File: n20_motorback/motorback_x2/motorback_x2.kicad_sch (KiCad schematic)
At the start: 13 parts, among them J1 Servo wire input, J2 Conn_01x01_Male, J3 Conn_01x01_Male, J4 prog_pins, U1 DRV8837DSGR, U2 ATtiny4-TS, U3 AIC1734-33GUTR

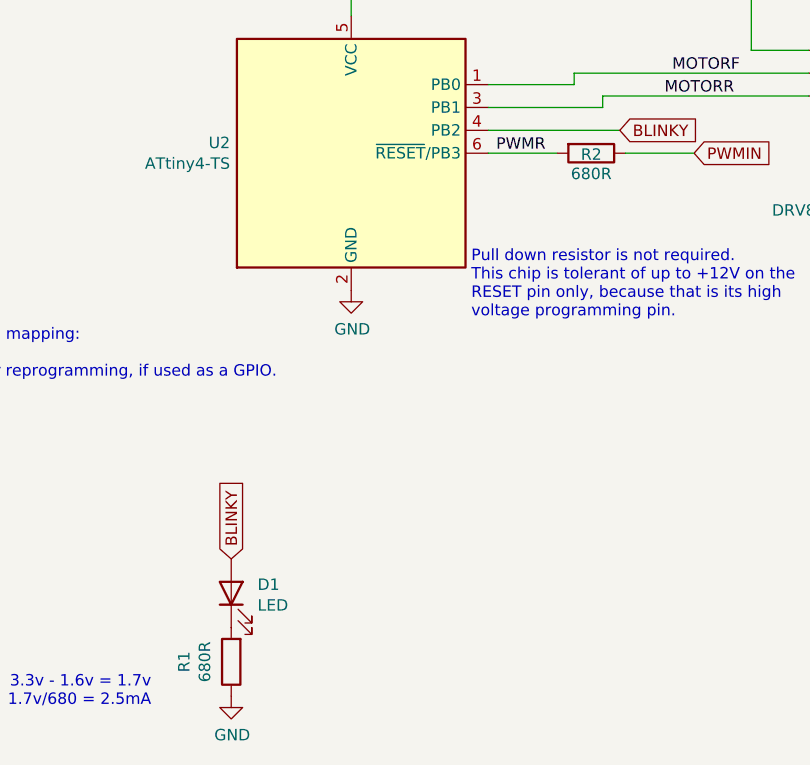
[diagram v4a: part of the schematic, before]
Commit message: Use 1k resistors
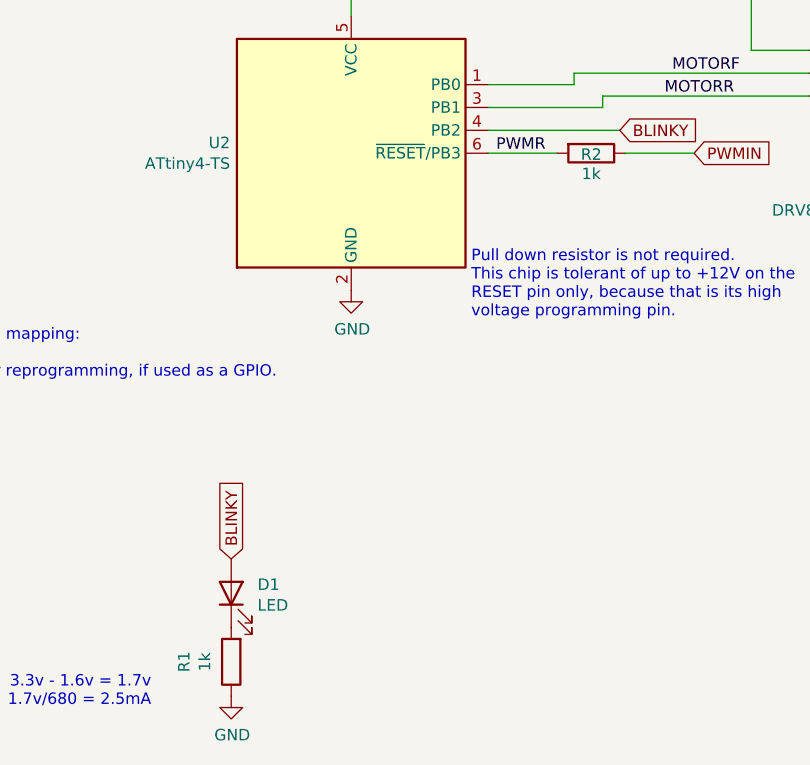
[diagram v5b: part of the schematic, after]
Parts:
- R1, R2: value 680R -> 1k; LCSC C23228 -> C21190
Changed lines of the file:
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@@
-(kicad_sch (version 20201015) (generator eeschema)
+(kicad_sch (version 20210126) (generator eeschema)
   (paper "A4")
   (title_block
@@
     (effects (font (size 1.27 1.27)) (justify left bottom))
   )
-  (global_label "PWMIN" (shape input) (at 40.64 43.18 0)    (property "Intersheet References" "${INTERSHEET_REFS}" (id 0) (at -12.7 -5.08 0)
-      (effects (font (size 1.27 1.27)) hide)
-    )
+  (global_label "PWMIN" (shape input) (at 40.64 43.18 0)
     (effects (font (size 1.27 1.27)) (justify left))
-  )
-  (global_label "PWMIN" (shape input) (at 44.45 86.36 0)    (property "Intersheet References" "${INTERSHEET_REFS}" (id 0) (at -8.89 38.1 0)
-      (effects (font (size 1.27 1.27)) hide)
-    )
+    (property "Intersheet References" "${INTERSHEET_REFS}" (id 0) (at -12.7 -5.08 0)
+      (effects (font (size 1.27 1.27)) hide)
+    )
+  )
+  (global_label "PWMIN" (shape input) (at 44.45 86.36 0)
     (effects (font (size 1.27 1.27)) (justify left))
-  )
-  (global_label "VBAT" (shape input) (at 66.04 38.1 90)    (property "Intersheet References" "${INTERSHEET_REFS}" (id 0) (at 0 0 0)
-      (effects (font (size 1.27 1.27)) hide)
-    )
+    (property "Intersheet References" "${INTERSHEET_REFS}" (id 0) (at -8.89 38.1 0)
+      (effects (font (size 1.27 1.27)) hide)
+    )
+  )
+  (global_label "VBAT" (shape input) (at 66.04 38.1 90)
     (effects (font (size 1.27 1.27)) (justify left))
-  )
-  (global_label "BLINKY" (shape input) (at 142.875 135.255 90)    (property "Intersheet References" "${INTERSHEET_REFS}" (id 0) (at 142.7956 124.726 90)
+    (property "Intersheet References" "${INTERSHEET_REFS}" (id 0) (at 0 0 0)
+      (effects (font (size 1.27 1.27)) hide)
+    )
+  )
+  (global_label "BLINKY" (shape input) (at 142.875 135.255 90)
+    (effects (font (size 1.27 1.27)) (justify left))
+    (property "Intersheet References" "${INTERSHEET_REFS}" (id 0) (at 142.7956 124.726 90)
       (effects (font (size 1.27 1.27)) (justify left) hide)
     )
+  )
+  (global_label "BLINKY" (shape input) (at 186.055 87.63 0)
     (effects (font (size 1.27 1.27)) (justify left))
-  )
-  (global_label "BLINKY" (shape input) (at 186.055 87.63 0)    (property "Intersheet References" "${INTERSHEET_REFS}" (id 0) (at 196.584 87.5506 0)
+    (property "Intersheet References" "${INTERSHEET_REFS}" (id 0) (at 196.584 87.5506 0)
       (effects (font (size 1.27 1.27)) (justify left) hide)
     )
+  )
+  (global_label "PWMIN" (shape input) (at 194.31 90.17 0)
     (effects (font (size 1.27 1.27)) (justify left))
-  )
-  (global_label "PWMIN" (shape input) (at 194.31 90.17 0)    (property "Intersheet References" "${INTERSHEET_REFS}" (id 0) (at 22.86 2.54 0)
-      (effects (font (size 1.27 1.27)) hide)
-    )
+    (property "Intersheet References" "${INTERSHEET_REFS}" (id 0) (at 22.86 2.54 0)
+      (effects (font (size 1.27 1.27)) hide)
+    )
+  )
+  (global_label "VBAT" (shape input) (at 233.045 58.42 0)
     (effects (font (size 1.27 1.27)) (justify left))
-  )
-  (global_label "VBAT" (shape input) (at 233.045 58.42 0)    (property "Intersheet References" "${INTERSHEET_REFS}" (id 0) (at 301.625 -158.75 0)
-      (effects (font (size 1.27 1.27)) hide)
-    )
-    (effects (font (size 1.27 1.27)) (justify left))
+    (property "Intersheet References" "${INTERSHEET_REFS}" (id 0) (at 301.625 -158.75 0)
+      (effects (font (size 1.27 1.27)) hide)
+    )
   )
   (symbol (lib_id "power:PWR_FLAG") (at 55.88 48.26 180) (unit 1)
@@
       (effects (font (size 1.27 1.27)) hide)
     )
+    (pin "1")
   )
   (symbol (lib_id "power:PWR_FLAG") (at 74.93 43.18 0) (unit 1)
@@
       (effects (font (size 1.27 1.27)) hide)
     )
+    (pin "1")
   )
   (symbol (lib_id "power:GND") (at 41.275 95.25 0) (unit 1)
@@
       (effects (font (size 1.27 1.27)) hide)
     )
+    (pin "1")
   )
   (symbol (lib_id "power:GND") (at 43.18 37.465 0) (unit 1)
@@
       (effects (font (size 1.27 1.27)) hide)
     )
+    (pin "1")
   )
   (symbol (lib_id "power:GND") (at 64.135 48.26 0) (unit 1)
@@
       (effects (font (size 1.27 1.27)) hide)
     )
+    (pin "1")
   )
   (symbol (lib_id "power:GND") (at 142.875 150.495 0) (unit 1)
@@
       (effects (font (size 1.27 1.27)) hide)
     )
+    (pin "1")
   )
   (symbol (lib_id "power:GND") (at 156.21 105.41 0) (unit 1)
@@
       (effects (font (size 1.27 1.27)) hide)
     )
+    (pin "1")
   )
   (symbol (lib_id "power:GND") (at 217.17 93.98 0) (unit 1)
@@
       (effects (font (size 1.27 1.27)) hide)
     )
+    (pin "1")
   )
   (symbol (lib_id "power:GND") (at 224.155 66.04 0) (unit 1)
@@
       (effects (font (size 1.27 1.27)) hide)
     )
+    (pin "1")
   )
   (symbol (lib_id "Connector:Conn_01x01_Male") (at 252.73 73.66 180) (unit 1)
@@
       (effects (font (size 1.27 1.27)) hide)
     )
+    (pin "1")
   )
   (symbol (lib_id "Connector:Conn_01x01_Male") (at 252.73 88.9 180) (unit 1)
@@
       (effects (font (size 1.27 1.27)) hide)
     )
+    (pin "1")
   )
   (symbol (lib_id "Device:R") (at 142.875 146.685 180) (unit 1)
     (in_bom yes) (on_board yes)
     (property "Reference" "R1" (id 0) (at 137.6488 146.685 90))
-    (property "Value" "680R" (id 1) (at 139.947 146.685 90))
+    (property "Value" "1k" (id 1) (at 139.947 146.685 90))
     (property "Footprint" "Resistor_SMD:R_0603_1608Metric" (id 2) (at 144.653 146.685 90)
       (effects (font (size 1.27 1.27)) hide)
@@
       (effects (font (size 1.27 1.27)) hide)
     )
-    (property "LCSC" "C23228" (id 4) (at 142.875 146.685 0)
-      (effects (font (size 1.27 1.27)) hide)
-    )
+    (property "LCSC" "C21190" (id 4) (at 142.875 146.685 0)
+      (effects (font (size 1.27 1.27)) hide)
+    )
+    (pin "1")
+    (pin "2")
   )
   (symbol (lib_id "Device:R") (at 182.88 90.17 270) (unit 1)
     (in_bom yes) (on_board yes)
     (property "Reference" "R2" (id 0) (at 182.88 90.3162 90))
-    (property "Value" "680R" (id 1) (at 182.88 92.463 90))
+    (property "Value" "1k" (id 1) (at 182.88 92.463 90))
     (property "Footprint" "Resistor_SMD:R_0603_1608Metric" (id 2) (at 182.88 88.392 90)
       (effects (font (size 1.27 1.27)) hide)
@@
       (effects (font (size 1.27 1.27)) hide)
     )
-    (property "LCSC" "C23228" (id 4) (at 182.88 90.17 0)
-      (effects (font (size 1.27 1.27)) hide)
-    )
+    (property "LCSC" "C21190" (id 4) (at 182.88 90.17 0)
+      (effects (font (size 1.27 1.27)) hide)
+    )
+    (pin "1")
+    (pin "2")
   )
   (symbol (lib_id "Device:LED") (at 142.875 139.065 90) (unit 1)
@@
       (effects (font (size 1.27 1.27)) hide)
     )
+    (pin "1")
+    (pin "2")
   )
   (symbol (lib_id "Device:C") (at 81.915 46.99 0) (unit 1)
@@
       (effects (font (size 1.27 1.27)) hide)
     )
+    (pin "1")
+    (pin "2")
   )
   (symbol (lib_id "Device:C") (at 114.3 46.99 0) (unit 1)
@@
       (effects (font (size 1.27 1.27)) hide)
     )
+    (pin "1")
+    (pin "2")
   )
   (symbol (lib_id "Device:C") (at 224.155 62.23 0) (unit 1)
@@
       (effects (font (size 1.27 1.27)) hide)
     )
+    (pin "1")
+    (pin "2")
   )
   (symbol (lib_id "motorback:Conn_01x03_withmechanical") (at 31.75 45.72 0) (mirror x) (unit 1)
@@
       (effects (font (size 1.27 1.27)) hide)
     )
+    (pin "1")
+    (pin "2")
+    (pin "3")
+    (pin "MP")
   )
   (symbol (lib_id "Connector:Conn_01x05_Male") (at 31.75 86.36 0) (mirror x) (unit 1)
@@
       (effects (font (size 1.27 1.27)) hide)
     )
+    (pin "1")
+    (pin "2")
+    (pin "3")
+    (pin "4")
+    (pin "5")
   )
   (symbol (lib_id "motorback:generic_regulator_GOI") (at 101.6 39.37 0) (unit 1)
@@
       (effects (font (size 1.27 1.27)) hide)
     )
+    (pin "1")
+    (pin "2")
+    (pin "3")
   )
   (symbol (lib_id "Driver_Motor:DRV8837") (at 217.17 81.28 0) (unit 1)
@@
       (effects (font (size 1.27 1.27)) hide)
     )
+    (pin "1")
+    (pin "2")
+    (pin "3")
+    (pin "4")
+    (pin "5")
+    (pin "6")
+    (pin "7")
+    (pin "8")
+    (pin "9")
   )
   (symbol (lib_id "MCU_Microchip_ATtiny:ATtiny4-TS") (at 156.21 90.17 0) (unit 1)
@@
       (effects (font (size 1.27 1.27)) hide)
     )
+    (pin "1")
+    (pin "2")
+    (pin "3")
+    (pin "4")
+    (pin "5")
+    (pin "6")
   )
   (sheet_instances
@@
     )
     (path "/668b33c0-eeaa-4f9d-b177-e9bb894eaa23"
-      (reference "R1") (unit 1) (value "680R") (footprint "Resistor_SMD:R_0603_1608Metric")
+      (reference "R1") (unit 1) (value "1k") (footprint "Resistor_SMD:R_0603_1608Metric")
     )
     (path "/92a7a6ba-5e73-468d-b3fe-9c3572a32afb"
-      (reference "R2") (unit 1) (value "680R") (footprint "Resistor_SMD:R_0603_1608Metric")
+      (reference "R2") (unit 1) (value "1k") (footprint "Resistor_SMD:R_0603_1608Metric")
     )
     (path "/17f044cf-d669-4296-9d52-0d1ba68a5a56"

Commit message: Complete routing latest variation
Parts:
- C1: MPN (none) -> CL10A106KP8NNNC; Manufacturer (none) -> Samsung Electro
- C2, C3: MPN (none) -> CL05A105KA5NQNC; Manufacturer (none) -> Samsung Electro
- D1: MPN (none) -> Red LED 0603; Manufacturer (none) -> Any
- J1: MPN (none) -> SM03B-SRSS-TB; Manufacturer (none) -> JST
- R1, R2: MPN (none) -> 1k ohm 0603; Manufacturer (none) -> Any
- U1: MPN (none) -> DRV8837DSGR; Manufacturer (none) -> TI
- U2: MPN (none) -> ATTINY4-TSHR; Manufacturer (none) -> Microchip
- U3: MPN (none) -> AIC1734-33GUTR; Manufacturer (none) -> AIC
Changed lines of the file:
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@@
+      (effects (font (size 1.27 1.27)) hide)
+    )
+    (property "MPN" "1k ohm 0603" (id 4) (at 142.875 146.685 0)
+      (effects (font (size 1.27 1.27)) hide)
+    )
+    (property "Manufacturer" "Any" (id 5) (at 142.875 146.685 0)
       (effects (font (size 1.27 1.27)) hide)
     )
@@
       (effects (font (size 1.27 1.27)) hide)
     )
+    (property "MPN" "1k ohm 0603" (id 4) (at 182.88 90.17 0)
+      (effects (font (size 1.27 1.27)) hide)
+    )
+    (property "Manufacturer" "Any" (id 5) (at 182.88 90.17 0)
+      (effects (font (size 1.27 1.27)) hide)
+    )
     (pin "1")
     (pin "2")
@@
       (effects (font (size 1.27 1.27)) hide)
     )
+    (property "MPN" "Red LED 0603" (id 4) (at 142.875 139.065 0)
+      (effects (font (size 1.27 1.27)) hide)
+    )
+    (property "Manufacturer" "Any" (id 5) (at 142.875 139.065 0)
+      (effects (font (size 1.27 1.27)) hide)
+    )
     (pin "1")
     (pin "2")
@@
       (effects (font (size 1.27 1.27)) hide)
     )
+    (property "MPN" "CL05A105KA5NQNC" (id 4) (at 81.915 46.99 0)
+      (effects (font (size 1.27 1.27)) hide)
+    )
+    (property "Manufacturer" "Samsung Electro" (id 5) (at 81.915 46.99 0)
+      (effects (font (size 1.27 1.27)) hide)
+    )
     (pin "1")
     (pin "2")
@@
       (effects (font (size 1.27 1.27)) hide)
     )
+    (property "MPN" "CL05A105KA5NQNC" (id 4) (at 114.3 46.99 0)
+      (effects (font (size 1.27 1.27)) hide)
+    )
+    (property "Manufacturer" "Samsung Electro" (id 5) (at 114.3 46.99 0)
+      (effects (font (size 1.27 1.27)) hide)
+    )
     (pin "1")
     (pin "2")
@@
       (effects (font (size 1.27 1.27)) hide)
     )
+    (property "MPN" "CL10A106KP8NNNC" (id 4) (at 224.155 62.23 0)
+      (effects (font (size 1.27 1.27)) hide)
+    )
+    (property "Manufacturer" "Samsung Electro" (id 5) (at 224.155 62.23 0)
+      (effects (font (size 1.27 1.27)) hide)
+    )
     (pin "1")
     (pin "2")
@@
     )
     (property "Datasheet" "~" (id 3) (at 31.75 45.72 0)
+      (effects (font (size 1.27 1.27)) hide)
+    )
+    (property "MPN" "SM03B-SRSS-TB" (id 4) (at 31.75 45.72 0)
+      (effects (font (size 1.27 1.27)) hide)
+    )
+    (property "Manufacturer" "JST" (id 5) (at 31.75 45.72 0)
       (effects (font (size 1.27 1.27)) hide)
     )
@@
       (effects (font (size 1.27 1.27)) hide)
     )
+    (property "MPN" "AIC1734-33GUTR" (id 4) (at 101.6 39.37 0)
+      (effects (font (size 1.27 1.27)) hide)
+    )
+    (property "Manufacturer" "AIC" (id 5) (at 101.6 39.37 0)
+      (effects (font (size 1.27 1.27)) hide)
+    )
     (pin "1")
     (pin "2")
@@
     )
     (property "LCSC" "C39159" (id 4) (at 217.17 81.28 0)
+      (effects (font (size 1.27 1.27)) hide)
+    )
+    (property "MPN" "DRV8837DSGR" (id 4) (at 217.17 81.28 0)
+      (effects (font (size 1.27 1.27)) hide)
+    )
+    (property "Manufacturer" "TI" (id 5) (at 217.17 81.28 0)
       (effects (font (size 1.27 1.27)) hide)
     )
@@
       (effects (font (size 1.27 1.27)) hide)
     )
+    (property "MPN" "ATTINY4-TSHR" (id 4) (at 156.21 90.17 0)
+      (effects (font (size 1.27 1.27)) hide)
+    )
+    (property "Manufacturer" "Microchip" (id 5) (at 156.21 90.17 0)
+      (effects (font (size 1.27 1.27)) hide)
+    )
